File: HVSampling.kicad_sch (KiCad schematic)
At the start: 11 parts, among them K4 SPU01L-05, U5 LM393, U6 4N35, U9 TLV6002

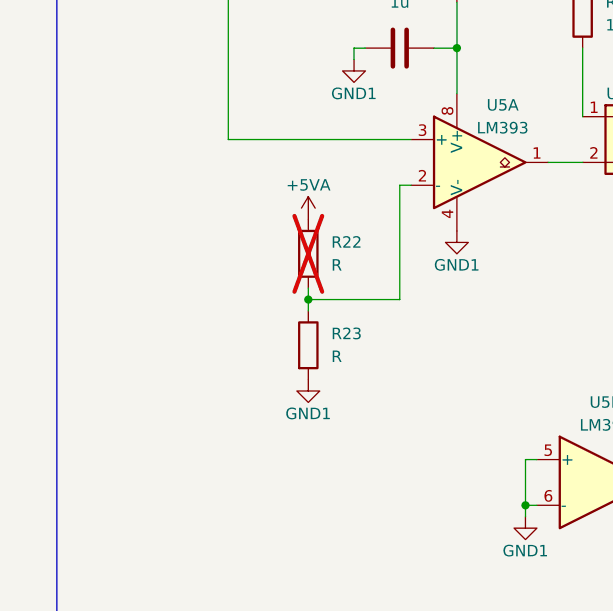
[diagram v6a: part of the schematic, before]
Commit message: *: Set precharge comparator threshold resistors and add capacitor
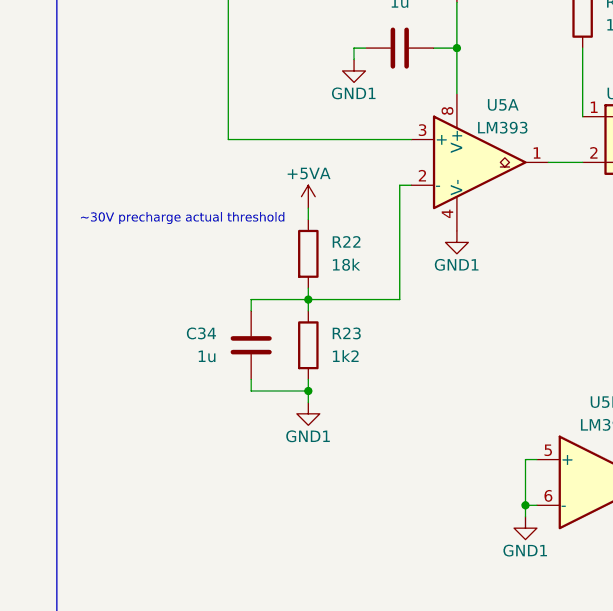
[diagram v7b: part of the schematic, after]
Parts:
- added C34: 1u, Capacitor_SMD:C_0603_1608Metric, symbol Device:C
- R22: value R -> 18k; now fitted
- R23: value R -> 1k2
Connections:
- net GND1: now also C34.1
- net at R22.2, R23.1, U5.2 (-): now also C34.2
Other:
- note added: "~30V precharge actual threshold"
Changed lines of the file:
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@@
+		)
+	)
+	(text "~30V precharge actual threshold"
+		(exclude_from_sim no)
+		(at 44.45 111.76 0)
+		(effects
+			(font
+				(size 1 1)
+			)
 		)
 	)
@@
 	)
 	(junction
+		(at 58.42 130.81)
+		(diameter 0)
+		(color 0 0 0 0)
+	)
+	(junction
 		(at 58.42 120.65)
 		(diameter 0)
@@
 	(wire
 		(pts
+			(xy 52.07 120.65) (xy 58.42 120.65)
+		)
+		(stroke
+			(width 0)
+			(type default)
+		)
+	)
+	(wire
+		(pts
 			(xy 58.42 119.38) (xy 58.42 120.65)
 		)
@@
 	(wire
 		(pts
+			(xy 52.07 130.81) (xy 58.42 130.81)
+		)
+		(stroke
+			(width 0)
+			(type default)
+		)
+	)
+	(wire
+		(pts
+			(xy 52.07 129.54) (xy 52.07 130.81)
+		)
+		(stroke
+			(width 0)
+			(type default)
+		)
+	)
+	(wire
+		(pts
 			(xy 85.09 105.41) (xy 88.9 105.41)
 		)
@@
 	(wire
 		(pts
+			(xy 58.42 110.49) (xy 58.42 111.76)
+		)
+		(stroke
+			(width 0)
+			(type default)
+		)
+	)
+	(wire
+		(pts
 			(xy 69.85 54.61) (xy 69.85 77.47)
 		)
@@
 	(wire
 		(pts
+			(xy 52.07 121.92) (xy 52.07 120.65)
+		)
+		(stroke
+			(width 0)
+			(type default)
+		)
+	)
+	(wire
+		(pts
 			(xy 105.41 106.68) (xy 105.41 100.33)
 		)
@@
 	(wire
 		(pts
+			(xy 58.42 132.08) (xy 58.42 130.81)
+		)
+		(stroke
+			(width 0)
+			(type default)
+		)
+	)
+	(wire
+		(pts
 			(xy 58.42 120.65) (xy 58.42 121.92)
 		)
@@
 		(pts
 			(xy 48.26 38.1) (xy 49.53 38.1)
+		)
+		(stroke
+			(width 0)
+			(type default)
+		)
+	)
+	(wire
+		(pts
+			(xy 58.42 130.81) (xy 58.42 129.54)
 		)
 		(stroke
@@
 	(symbol
 		(lib_id "power:GND1")
-		(at 58.42 129.54 0)
+		(at 58.42 132.08 0)
 		(unit 1)
 		(exclude_from_sim no)
@@
 		(dnp no)
 		(property "Reference" "#PWR064"
+			(at 58.42 138.43 0)
+			(effects
+				(font
+					(size 1.27 1.27)
+				)
+				(hide yes)
+			)
+		)
+		(property "Value" "GND1"
 			(at 58.42 135.89 0)
 			(effects
@@
 					(size 1.27 1.27)
 				)
-				(hide yes)
-			)
-		)
-		(property "Value" "GND1"
-			(at 58.42 133.35 0)
-			(effects
-				(font
-					(size 1.27 1.27)
-				)
 			)
 		)
 		(property "Footprint" ""
-			(at 58.42 129.54 0)
+			(at 58.42 132.08 0)
 			(effects
 				(font
@@
 		)
 		(property "Datasheet" ""
-			(at 58.42 129.54 0)
+			(at 58.42 132.08 0)
 			(effects
 				(font
@@
 		)
 		(property "Description" "Power symbol creates a global label with name \"GND1\" , ground"
-			(at 58.42 129.54 0)
+			(at 58.42 132.08 0)
 			(effects
 				(font
@@
 	(symbol
 		(lib_id "power:+5VA")
-		(at 58.42 111.76 0)
+		(at 58.42 110.49 0)
 		(unit 1)
 		(exclude_from_sim no)
@@
 		(dnp no)
 		(property "Reference" "#PWR063"
-			(at 58.42 115.57 0)
+			(at 58.42 114.3 0)
 			(effects
 				(font
@@
 		)
 		(property "Value" "+5VA"
-			(at 58.42 107.95 0)
+			(at 58.42 106.68 0)
 			(effects
 				(font
@@
 		)
 		(property "Footprint" ""
-			(at 58.42 111.76 0)
+			(at 58.42 110.49 0)
 			(effects
 				(font
@@
 		)
 		(property "Datasheet" ""
-			(at 58.42 111.76 0)
+			(at 58.42 110.49 0)
 			(effects
 				(font
@@
 		)
 		(property "Description" "Power symbol creates a global label with name \"+5VA\""
-			(at 58.42 111.76 0)
+			(at 58.42 110.49 0)
 			(effects
 				(font
@@
 			)
 		)
-		(property "Value" "R"
+		(property "Value" "1k2"
 			(at 60.96 126.9999 0)
 			(effects
@@
 				(path "/c467677d-b98c-4488-bd11-965ef67263b2/5111e28e-8231-41c0-b506-a567affaf28a"
 					(reference "#PWR072")
+					(unit 1)
+				)
+			)
+		)
+	)
+	(symbol
+		(lib_id "Device:C")
+		(at 52.07 125.73 0)
+		(mirror x)
+		(unit 1)
+		(exclude_from_sim no)
+		(in_bom yes)
+		(on_board yes)
+		(dnp no)
+		(property "Reference" "C34"
+			(at 48.26 124.4599 0)
+			(effects
+				(font
+					(size 1.27 1.27)
+				)
+				(justify right)
+			)
+		)
+		(property "Value" "1u"
+			(at 48.26 126.9999 0)
+			(effects
+				(font
+					(size 1.27 1.27)
+				)
+				(justify right)
+			)
+		)
+		(property "Footprint" "Capacitor_SMD:C_0603_1608Metric"
+			(at 53.0352 121.92 0)
+			(effects
+				(font
+					(size 1.27 1.27)
+				)
+				(hide yes)
+			)
+		)
+		(property "Datasheet" "~"
+			(at 52.07 125.73 0)
+			(effects
+				(font
+					(size 1.27 1.27)
+				)
+				(hide yes)
+			)
+		)
+		(property "Description" ""
+			(at 52.07 125.73 0)
+			(effects
+				(font
+					(size 1.27 1.27)
+				)
+				(hide yes)
+			)
+		)
+		(property "Dist" "LCSC"
+			(at 52.07 125.73 90)
+			(effects
+				(font
+					(size 1.27 1.27)
+				)
+				(hide yes)
+			)
+		)
+		(property "Dist #" "C5199872"
+			(at 52.07 125.73 90)
+			(effects
+				(font
+					(size 1.27 1.27)
+				)
+				(hide yes)
+			)
+		)
+		(property "Mfr" "Samsung"
+			(at 52.07 125.73 90)
+			(effects
+				(font
+					(size 1.27 1.27)
+				)
+				(hide yes)
+			)
+		)
+		(property "Mfr #" "CL10B105KB8NQNC"
+			(at 52.07 125.73 90)
+			(effects
+				(font
+					(size 1.27 1.27)
+				)
+				(hide yes)
+			)
+		)
+		(pin "1"
+		)
+		(pin "2"
+		)
+		(instances
+			(project "Precharge_PCB"
+				(path "/c467677d-b98c-4488-bd11-965ef67263b2/5111e28e-8231-41c0-b506-a567affaf28a"
+					(reference "C34")
 					(unit 1)
 				)
@@
 		(in_bom yes)
 		(on_board yes)
-		(dnp yes)
+		(dnp no)
 		(fields_autoplaced yes)
 		(property "Reference" "R22"
@@
 			)
 		)
-		(property "Value" "R"
+		(property "Value" "18k"
 			(at 60.96 116.8399 0)
 			(effects
